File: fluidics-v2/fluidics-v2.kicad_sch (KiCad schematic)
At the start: 25 parts, among them J1 PJ-063AH, J10 87832-1010, J11 87832-1010, J12 87832-1010, J13 0533980671, J14 0533980671, J15 A-DS_15_A_KG-T4S, J2 0705430001, J3 0705430001, J4 0705430001, J5 0705430001, J6 0705430001, J7 1860280, J8 87832-1010, J9 87832-1010, U2 Teensy4.1

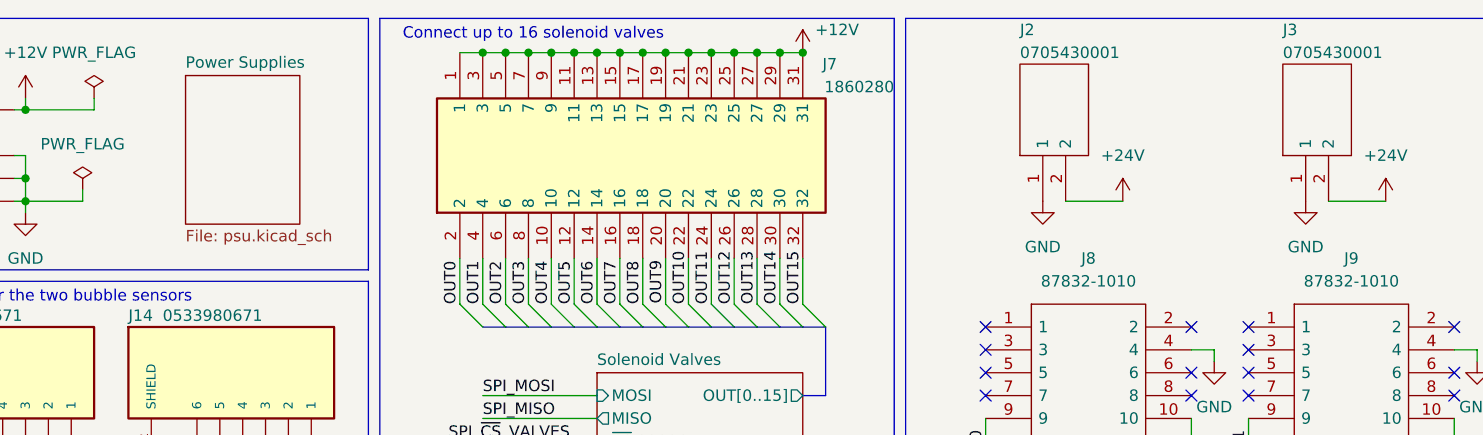
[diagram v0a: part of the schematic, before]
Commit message: updated text and schematic PDF
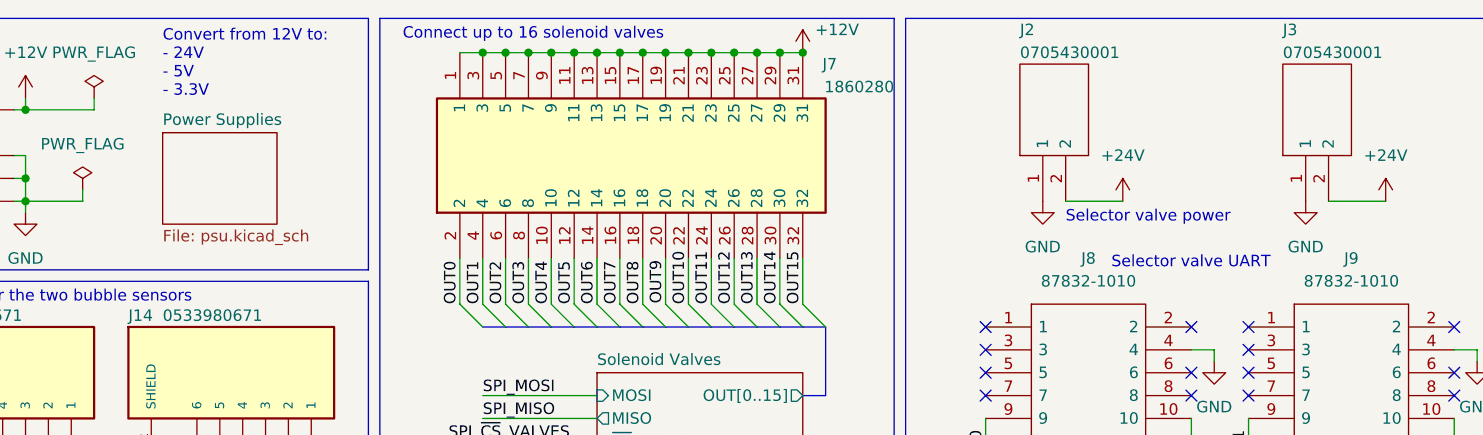
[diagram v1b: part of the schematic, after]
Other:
- note added: "Convert from 12V to: - 24V - 5V - 3.3V"
- note added: "Selector valve UART"
- note added: "Selector valve power"
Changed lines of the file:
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@@
+    (effects (font (size 1.27 1.27)) (justify left bottom))
+  )
+  (text "Convert from 12V to:\n- 24V\n- 5V\n- 3.3V" (at 46.99 21.59 0)
     (effects (font (size 1.27 1.27)) (justify left bottom))
   )
@@
   )
   (text "Syringe pump connector" (at 26.67 156.21 0)
+    (effects (font (size 1.27 1.27)) (justify left bottom))
+  )
+  (text "Selector valve UART" (at 152.4 40.64 0)
+    (effects (font (size 1.27 1.27)) (justify left bottom))
+  )
+  (text "Selector valve power" (at 147.32 35.56 0)
     (effects (font (size 1.27 1.27)) (justify left bottom))
   )
@@
     )
   )
-  (sheet (at 49.53 19.05) (size 12.7 16.51) (fields_autoplaced)
+  (sheet (at 46.99 25.4) (size 12.7 10.16) (fields_autoplaced)
     (stroke (width 0.1524) (type solid))
     (fill (color 0 0 0 0.0000))
-    (property "Sheetname" "Power Supplies" (at 49.53 18.3384 0)
+    (property "Sheetname" "Power Supplies" (at 46.99 24.6884 0)
       (effects (font (size 1.27 1.27)) (justify left bottom))
     )
-    (property "Sheetfile" "psu.kicad_sch" (at 49.53 36.1446 0)
+    (property "Sheetfile" "psu.kicad_sch" (at 46.99 36.1446 0)
       (effects (font (size 1.27 1.27)) (justify left top))
     )

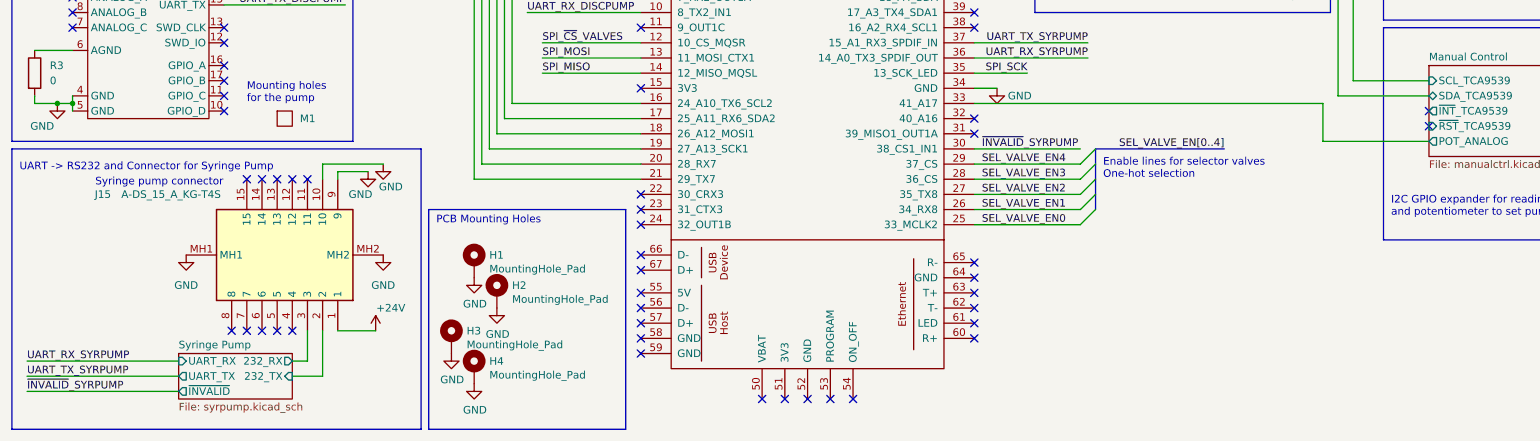
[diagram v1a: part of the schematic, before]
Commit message: added missing footprint
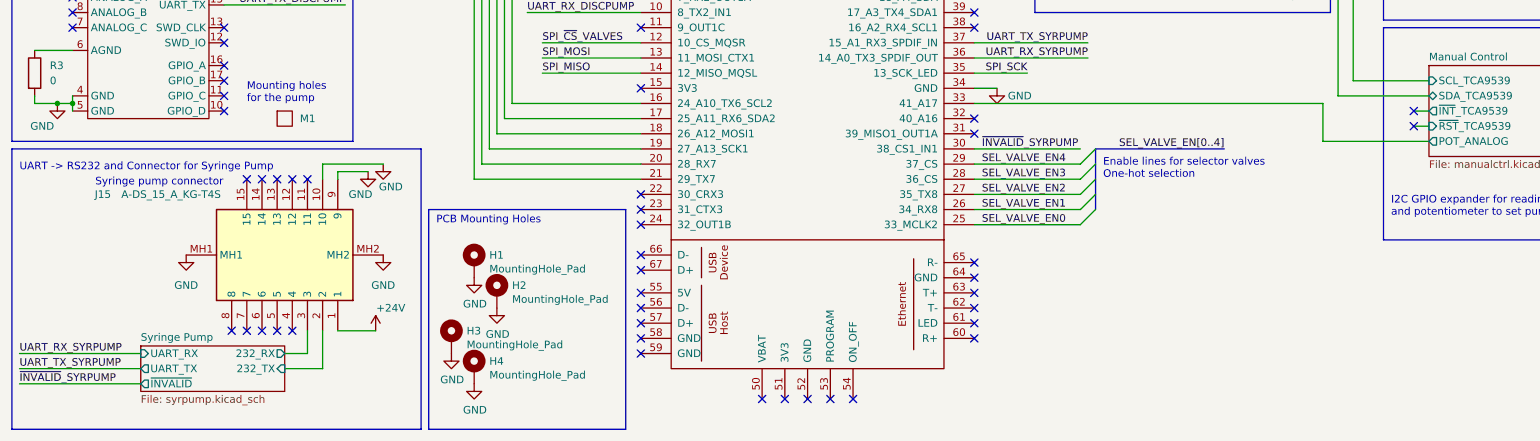
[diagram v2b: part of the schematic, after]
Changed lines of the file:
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@@
   (no_connect (at 149.86 191.77))
   (no_connect (at 161.29 54.61))
-  (no_connect (at 250.19 146.05))
+  (no_connect (at 247.65 146.05))
   (no_connect (at 48.26 135.89))
   (no_connect (at 173.99 176.53))
@@
   (no_connect (at 53.34 62.23))
   (no_connect (at 196.85 52.07))
-  (no_connect (at 250.19 143.51))
+  (no_connect (at 247.65 143.51))
   (no_connect (at 118.11 170.18))
   (no_connect (at 57.15 154.94))
@@
     (stroke (width 0) (type default))
   )
-  (wire (pts (xy 62.23 185.42) (xy 62.23 180.34))
+  (wire (pts (xy 62.23 184.15) (xy 62.23 180.34))
     (stroke (width 0) (type default))
   )
@@
     (stroke (width 0) (type default))
   )
+  (wire (pts (xy 247.65 143.51) (xy 250.19 143.51))
+    (stroke (width 0) (type default))
+  )
   (wire (pts (xy 138.43 57.15) (xy 138.43 67.31))
     (stroke (width 0) (type default))
@@
     (stroke (width 0) (type default))
   )
-  (wire (pts (xy 15.24 187.96) (xy 40.64 187.96))
-    (stroke (width 0) (type default))
-  )
   (wire (pts (xy 85.09 16.51) (xy 87.63 16.51))
     (stroke (width 0) (type default))
@@
     (stroke (width 0) (type default))
   )
-  (wire (pts (xy 15.24 190.5) (xy 40.64 190.5))
+  (wire (pts (xy 13.97 189.23) (xy 34.29 189.23))
     (stroke (width 0) (type default))
   )
@@
     (stroke (width 0) (type default))
   )
+  (wire (pts (xy 34.29 186.69) (xy 13.97 186.69))
+    (stroke (width 0) (type default))
+  )
   (wire (pts (xy 99.06 127) (xy 118.11 127))
     (stroke (width 0) (type default))
@@
     (stroke (width 0) (type default))
   )
-  (wire (pts (xy 59.69 187.96) (xy 64.77 187.96))
+  (wire (pts (xy 58.42 186.69) (xy 64.77 186.69))
     (stroke (width 0) (type default))
   )
@@
     (stroke (width 0) (type default))
   )
-  (wire (pts (xy 15.24 185.42) (xy 40.64 185.42))
-    (stroke (width 0) (type default))
-  )
   (wire (pts (xy 234.95 124.46) (xy 241.3 124.46))
     (stroke (width 0) (type default))
@@
     (stroke (width 0) (type default))
   )
-  (wire (pts (xy 59.69 185.42) (xy 62.23 185.42))
+  (wire (pts (xy 58.42 184.15) (xy 62.23 184.15))
     (stroke (width 0) (type default))
   )
@@
     (stroke (width 0) (type default))
   )
+  (wire (pts (xy 34.29 184.15) (xy 13.97 184.15))
+    (stroke (width 0) (type default))
+  )
   (bus (pts (xy 92.71 46.99) (xy 95.25 46.99))
     (stroke (width 0) (type default))
@@
     (stroke (width 0) (type default))
   )
+  (wire (pts (xy 247.65 146.05) (xy 250.19 146.05))
+    (stroke (width 0) (type default))
+  )
   (wire (pts (xy 87.63 16.51) (xy 90.17 16.51))
     (stroke (width 0) (type default))
@@
     (stroke (width 0) (type default))
   )
-  (wire (pts (xy 64.77 187.96) (xy 64.77 180.34))
+  (wire (pts (xy 64.77 186.69) (xy 64.77 180.34))
     (stroke (width 0) (type default))
   )
@@
     (effects (font (size 1.27 1.27)) (justify left bottom))
   )
-  (label "~{INVALID}_SYRPUMP" (at 15.24 190.5 0) (fields_autoplaced)
+  (label "~{INVALID}_SYRPUMP" (at 13.97 189.23 0) (fields_autoplaced)
     (effects (font (size 1.27 1.27)) (justify left bottom))
   )
-  (label "UART_RX_SYRPUMP" (at 15.24 185.42 0) (fields_autoplaced)
+  (label "UART_RX_SYRPUMP" (at 13.97 184.15 0) (fields_autoplaced)
     (effects (font (size 1.27 1.27)) (justify left bottom))
   )
@@
     (effects (font (size 1.27 1.27)) (justify right bottom))
   )
-  (label "UART_TX_SYRPUMP" (at 15.24 187.96 0) (fields_autoplaced)
+  (label "UART_TX_SYRPUMP" (at 13.97 186.69 0) (fields_autoplaced)
     (effects (font (size 1.27 1.27)) (justify left bottom))
   )
@@
     )
   )
-  (sheet (at 40.64 184.15) (size 19.05 7.62) (fields_autoplaced)
+  (sheet (at 34.29 182.88) (size 24.13 7.62) (fields_autoplaced)
     (stroke (width 0.1524) (type solid))
     (fill (color 0 0 0 0.0000))
-    (property "Sheetname" "Syringe Pump" (at 40.64 183.4384 0)
+    (property "Sheetname" "Syringe Pump" (at 34.29 182.1684 0)
       (effects (font (size 1.27 1.27)) (justify left bottom))
     )
-    (property "Sheetfile" "syrpump.kicad_sch" (at 40.64 192.3546 0)
+    (property "Sheetfile" "syrpump.kicad_sch" (at 34.29 191.0846 0)
       (effects (font (size 1.27 1.27)) (justify left top))
     )
-    (pin "~{INVALID}" output (at 40.64 190.5 180)
+    (pin "~{INVALID}" output (at 34.29 189.23 180)
       (effects (font (size 1.27 1.27)) (justify left))
     )
-    (pin "232_TX" input (at 59.69 187.96 0)
+    (pin "232_TX" input (at 58.42 186.69 0)
       (effects (font (size 1.27 1.27)) (justify right))
     )
-    (pin "232_RX" output (at 59.69 185.42 0)
+    (pin "232_RX" output (at 58.42 184.15 0)
       (effects (font (size 1.27 1.27)) (justify right))
     )
-    (pin "UART_TX" output (at 40.64 187.96 180)
+    (pin "UART_TX" output (at 34.29 186.69 180)
       (effects (font (size 1.27 1.27)) (justify left))
     )
-    (pin "UART_RX" input (at 40.64 185.42 180)
+    (pin "UART_RX" input (at 34.29 184.15 180)
       (effects (font (size 1.27 1.27)) (justify left))
     )

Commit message: new version
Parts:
- added C4: 0.01u, Capacitor_SMD:C_0603_1608Metric, symbol Device:C
- added J17, J18: 0533980671, molex_connectors:MOLEX_0533980671, symbol 0533980671:0533980671
- added TP1, TP2: TestPoint_2Pole, TestPoint:TestPoint_2Pads_Pitch2.54mm_Drill0.8mm, symbol Connector:TestPoint_2Pole
- added U11: LTC4311CSC6-TRPBF, SOT-6_SC_LIT, symbol LTC4311CSC6#TRPBF:LTC4311CSC6-TRPBF
- R1, R2: value 1k -> 10k
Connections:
- net +3.3V: now also C4.1, J17.4, J18.4, U11.1 (VCC), U11.3 (ENABLE)
- net GND: now also C4.2, J17.3, J17.S1 (SHIELD), J17.S2 (SHIELD), J18.3, J18.S1 (SHIELD), J18.S2 (SHIELD), U11.2 (GND), U11.5 (GND)
- net I2C_SCL: now also J17.2, TP1.1, U11.4 (BUS2)
- net I2C_SDA: now also J17.5, TP1.2, U11.6 (BUS1)
- net Selector Valves/SDA 5V: now reaches J12.1
- net Selector Valves/SDA 5V: now also J10.1, J11.1, J8.1, J9.1, TP2.1
- net Selector Valves/SCL 5V: now reaches J12.2
- net Selector Valves/SCL 5V: now also J10.2, J11.2, J8.2, J9.2, TP2.2
- net Manual Control/POT_ANALOG renamed POT_ANALOG
- net RX50: no longer names the net of J8.10
- net RX51: no longer names the net of J9.10
- net RX52: no longer names the net of J10.10
- net RX53: no longer names the net of J11.10
- net RX54: no longer names the net of J12.10
- net SEL_VALVE_EN0: no longer names the net of U2.25 (33_MCLK2)
- net SEL_VALVE_EN1 renamed ~{CS}3
- net SEL_VALVE_EN2 renamed ~{CS}2
- net SEL_VALVE_EN3 renamed ~{CS}1
- net SEL_VALVE_EN4 renamed ~{CS}0
- net TX50: no longer names the net of J8.9
- net TX51: no longer names the net of J9.9
- net TX52: no longer names the net of J10.9
- net TX53: no longer names the net of J11.9
- net TX54: no longer names the net of J12.9
- net UART_RX_SEL_VALVE: no longer names the net of U2.3 (1_TX1_CTX2_MISO1)
- net UART_TX_SEL_VALVE: no longer names the net of U2.2 (0_RX1_CRX2_CS1)
- new net Sensors/SCL_OUT: J18.2
- new net Sensors/SDA_OUT: J18.5
- no-connect marks 99 -> 106
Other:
- sheet I2C Sensors renamed Sensors
- sheet Selector Valves ports: added SCL 3.3V, SCL 5V, SDA 3.3V, SDA 5V; removed EN[0..4], RX3.3, RX5[0..4], TX3.3, TX5[0..4]
- sheet Sensors ports: added MISO, SCK, SCL_IN, SCL_OUT, SDA_IN, SDA_OUT, ~{CS}[0..3]; removed SCL_TCA9539, SDA_TCA9539
- note added: "Four air pressure sensors, two flow sensors"
- note added: "I2C Active Driver Drive higher capacitive loads (more devices, longer connectors)"
- note added: "I2C Addresses: 0x74: GPIO expander 0x08: Flow sensor 0x--: Selector Valve(s) (configurable)"
- note added: "I2C connections for flow sensors"
- note added: "Include test points for I2C before and after level shifting"
- note removed: "Connections for up to 5 selector valves - all use UART"
- note removed: "Enable lines for selector valves One-hot selection"
- note removed: "I2C Pullup Resistors https://www.ti.com/lit/an/slva689/slva689.pdf 4 devices in normal mode -> 1.2 nF bus capacitance worst case 1000 ns rise time Use 1k resistors Addresses: 0x74: GPIO expander 0x08: Flow sensor 0x28: Pressure Sensor 1 0x62: Pressure Sensor 2"
- note removed: "Selector valve UART"
- note removed: "Syringe pump connector"
- note removed: "Two pressure sensors, one flow sensor"
- moved on the sheet: H1, H2, H3, H4, J10, J11, J12, J15, J2, J3, J4, J5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

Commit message: started layout
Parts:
- removed J7: 1860280, phoenix_2:1860280, symbol 1860280:1860280
- added J5: 1860280, phoenix_2:1860280, symbol 1860280:1860280
- added TP3: TestPoint, TestPoint:TestPoint_THTPad_1.5x1.5mm_Drill0.7mm, symbol Connector:TestPoint
- renumbered C4 to C?, H3 to H1, H1 to H2, H4 to H3, H2 to H4, J4 to J11, J11 to J12, J5 to J13, J17 to J14, J12 to J15, J6 to J16, J18 to J17, J13 to J2, J15 to J3, J14 to J4, J8 to J6, J2 to J7, J9 to J8, J3 to J9, R3 to R1, R1 to R2, R2 to R3, U11 to U3
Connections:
- net +12V: now also J5.10, J5.12, J5.14, J5.16, J5.18, J5.2, J5.20, J5.22, J5.24, J5.26, J5.28, J5.30, J5.32, J5.4, J5.6, J5.8
- net GND: now also TP3.1
- net OUT0: now also J5.1
- net OUT1: now also J5.3
- net OUT10: now also J5.21
- net OUT11: now also J5.23
- net OUT12: now also J5.25
- net OUT13: now also J5.27
- net OUT14: now also J5.29
- net OUT15: now also J5.31
- net OUT2: now also J5.5
- net OUT3: now also J5.7
- net OUT4: now also J5.9
- net OUT5: now also J5.11
- net OUT6: now also J5.13
- net OUT7: now also J5.15
- net OUT8: now also J5.17
- net OUT9: now also J5.19
